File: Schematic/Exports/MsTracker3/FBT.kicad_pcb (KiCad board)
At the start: 2 copper layers, 42.8 x 122.5 mm, 23 parts, among them J1 TRRS Connector 3.5, J2 TRRS Connector 3.5, SW1 SW_SPDT, U1 HT7333-1-TO92

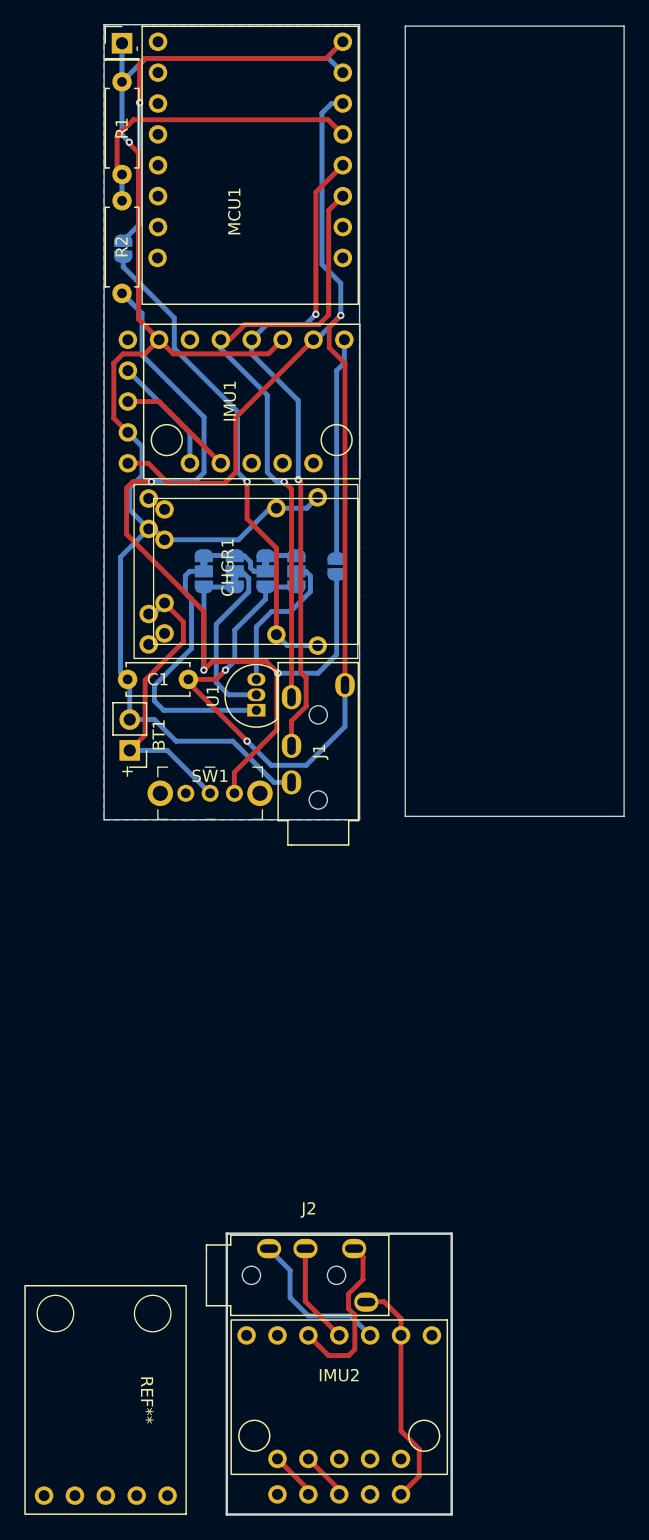
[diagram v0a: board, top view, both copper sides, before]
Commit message: Export the next revision of PCBs for fabrication
Made at JLCPCB
Also picked apart the LSM6DS3 datasheet some more. Apparently, the auto hard/soft iron compensation isn't dynamic. It depends on pre-calculated matrices fed into the IMU's registers.
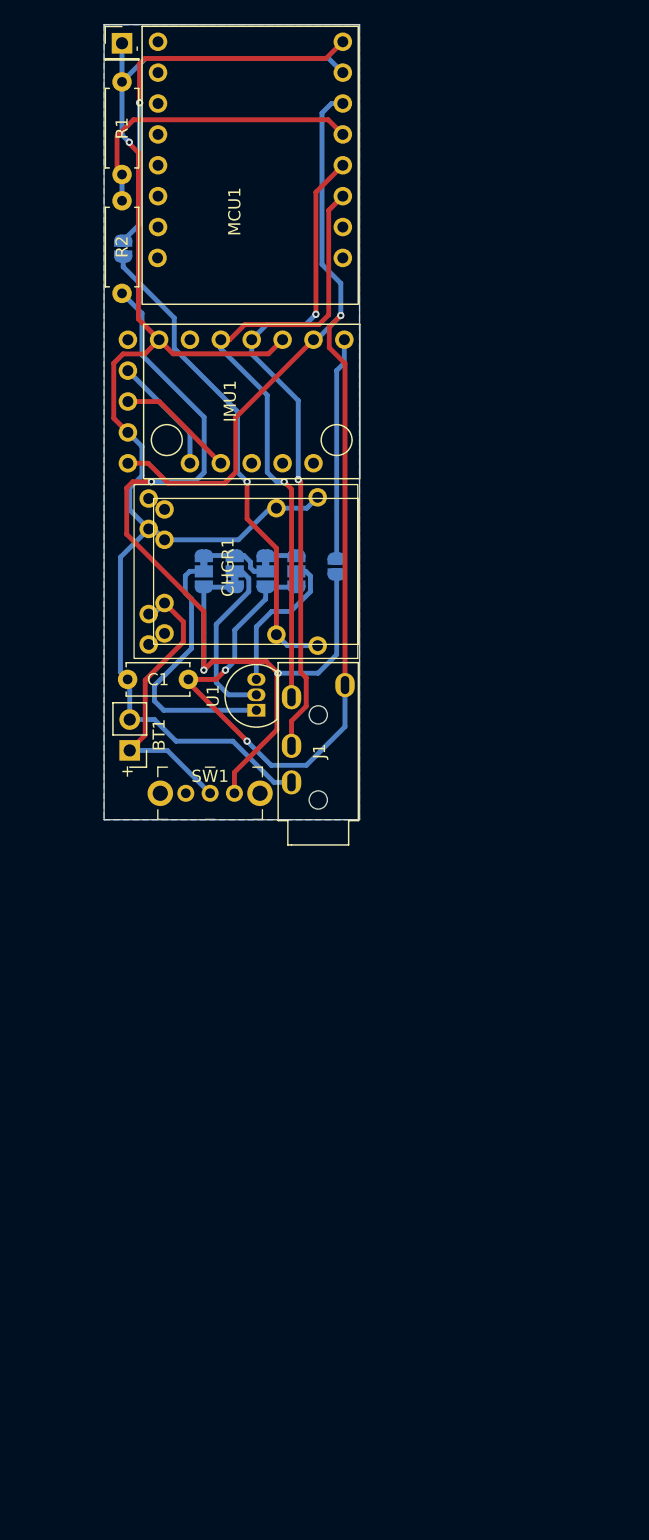
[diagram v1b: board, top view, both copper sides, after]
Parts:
- removed GY2: ~, My_Library:GY-271
- removed IMU2: ~, My_Library:GY-BMI160
- removed J2: TRRS Connector 3.5, My_Library:PJ-320A
- removed REF**: GY-273, My_Library:GY-273
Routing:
- net ESP32_3V3: track 131.1 -> 112.0 mm
- net SDA_1: track 66.2 -> 52.1 mm
- net GND: track 139.6 -> 127.0 mm
- net SCL_1: track 63.3 -> 55.1 mm
- net Net-(GY2-SCL): track 3.97 -> 0.00 mm
- net Net-(GY2-SDA): track 3.97 -> 0.00 mm
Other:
- board size 42.8 x 122.5 mm -> 21 x 65.4 mm
- board text removed: "Type B Rev. 1.0"
